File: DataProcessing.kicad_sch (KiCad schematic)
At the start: 2 parts, among them J3 AVR-ISP-6, U2 ATmega328PB-M

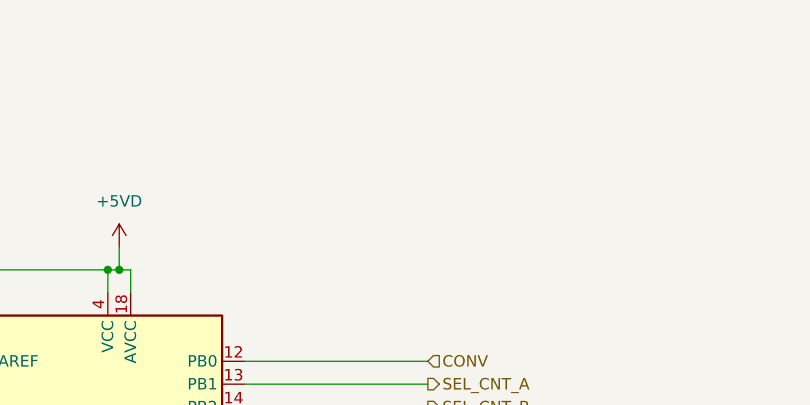
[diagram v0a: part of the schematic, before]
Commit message: added decoupling Cs
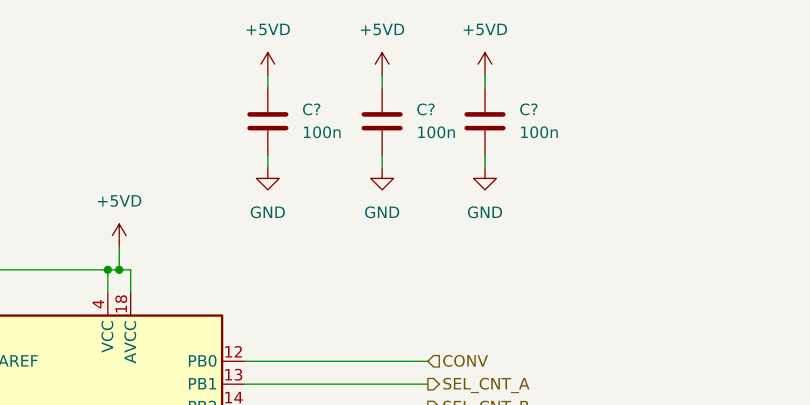
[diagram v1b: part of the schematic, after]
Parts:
- added C? (x3): 100n, Capacitor_SMD:C_0603_1608Metric, symbol Device:C
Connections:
- net +5VD: now also C?.1, C?.1, C?.1
- net GND: now also C?.2, C?.2, C?.2
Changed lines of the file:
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@@
   (junction (at 92.71 53.34) (diameter 0) (color 0 0 0 0)
   )
+  (wire (pts (xy 121.92 40.64) (xy 121.92 41.91))
+    (stroke (width 0) (type default) (color 0 0 0 0))
+  )
+  (wire (pts (xy 133.35 31.75) (xy 133.35 33.02))
+    (stroke (width 0) (type default) (color 0 0 0 0))
+  )
   (wire (pts (xy 74.93 53.34) (xy 91.44 53.34))
     (stroke (width 0) (type default) (color 0 0 0 0))
@@
     (stroke (width 0) (type default) (color 0 0 0 0))
   )
+  (wire (pts (xy 109.22 40.64) (xy 109.22 41.91))
+    (stroke (width 0) (type default) (color 0 0 0 0))
+  )
   (wire (pts (xy 91.44 55.88) (xy 91.44 53.34))
     (stroke (width 0) (type default) (color 0 0 0 0))
@@
     (stroke (width 0) (type default) (color 0 0 0 0))
   )
+  (wire (pts (xy 121.92 31.75) (xy 121.92 33.02))
+    (stroke (width 0) (type default) (color 0 0 0 0))
+  )
   (wire (pts (xy 106.68 109.22) (xy 127 109.22))
     (stroke (width 0) (type default) (color 0 0 0 0))
@@
     (stroke (width 0) (type default) (color 0 0 0 0))
   )
+  (wire (pts (xy 133.35 40.64) (xy 133.35 41.91))
+    (stroke (width 0) (type default) (color 0 0 0 0))
+  )
   (wire (pts (xy 106.68 106.68) (xy 127 106.68))
     (stroke (width 0) (type default) (color 0 0 0 0))
@@
   )
   (wire (pts (xy 106.68 96.52) (xy 127 96.52))
+    (stroke (width 0) (type default) (color 0 0 0 0))
+  )
+  (wire (pts (xy 109.22 31.75) (xy 109.22 33.02))
     (stroke (width 0) (type default) (color 0 0 0 0))
   )
@@
     (effects (font (size 1.27 1.27)) (justify left))
   )
+  (symbol (lib_id "power:GND") (at 109.22 41.91 0) (unit 1)
+    (in_bom yes) (on_board yes) (fields_autoplaced)
+    (property "Reference" "#PWR?" (id 0) (at 109.22 48.26 0)
+      (effects (font (size 1.27 1.27)) hide)
+    )
+    (property "Value" "GND" (id 1) (at 109.22 46.99 0))
+    (property "Footprint" "" (id 2) (at 109.22 41.91 0)
+      (effects (font (size 1.27 1.27)) hide)
+    )
+    (property "Datasheet" "" (id 3) (at 109.22 41.91 0)
+      (effects (font (size 1.27 1.27)) hide)
+    )
+    (pin "1")
+  )
+  (symbol (lib_id "power:+5VD") (at 109.22 31.75 0) (unit 1)
+    (in_bom yes) (on_board yes) (fields_autoplaced)
+    (property "Reference" "#PWR?" (id 0) (at 109.22 35.56 0)
+      (effects (font (size 1.27 1.27)) hide)
+    )
+    (property "Value" "+5VD" (id 1) (at 109.22 26.67 0))
+    (property "Footprint" "" (id 2) (at 109.22 31.75 0)
+      (effects (font (size 1.27 1.27)) hide)
+    )
+    (property "Datasheet" "" (id 3) (at 109.22 31.75 0)
+      (effects (font (size 1.27 1.27)) hide)
+    )
+    (pin "1")
+  )
+  (symbol (lib_id "Device:C") (at 121.92 36.83 0) (unit 1)
+    (in_bom yes) (on_board yes) (fields_autoplaced)
+    (property "Reference" "C?" (id 0) (at 125.73 35.5599 0)
+      (effects (font (size 1.27 1.27)) (justify left))
+    )
+    (property "Value" "100n" (id 1) (at 125.73 38.0999 0)
+      (effects (font (size 1.27 1.27)) (justify left))
+    )
+    (property "Footprint" "Capacitor_SMD:C_0603_1608Metric" (id 2) (at 122.8852 40.64 0)
+      (effects (font (size 1.27 1.27)) hide)
+    )
+    (property "Datasheet" "~" (id 3) (at 121.92 36.83 0)
+      (effects (font (size 1.27 1.27)) hide)
+    )
+    (pin "1")
+    (pin "2")
+  )
   (symbol (lib_id "power:+5VD") (at 232.41 40.64 0) (unit 1)
     (in_bom yes) (on_board yes) (fields_autoplaced)
@@
     )
     (property "Datasheet" "" (id 3) (at 91.44 139.7 0)
+      (effects (font (size 1.27 1.27)) hide)
+    )
+    (pin "1")
+  )
+  (symbol (lib_id "Device:C") (at 133.35 36.83 0) (unit 1)
+    (in_bom yes) (on_board yes) (fields_autoplaced)
+    (property "Reference" "C?" (id 0) (at 137.16 35.5599 0)
+      (effects (font (size 1.27 1.27)) (justify left))
+    )
+    (property "Value" "100n" (id 1) (at 137.16 38.0999 0)
+      (effects (font (size 1.27 1.27)) (justify left))
+    )
+    (property "Footprint" "Capacitor_SMD:C_0603_1608Metric" (id 2) (at 134.3152 40.64 0)
+      (effects (font (size 1.27 1.27)) hide)
+    )
+    (property "Datasheet" "~" (id 3) (at 133.35 36.83 0)
+      (effects (font (size 1.27 1.27)) hide)
+    )
+    (pin "1")
+    (pin "2")
+  )
+  (symbol (lib_id "Device:C") (at 109.22 36.83 0) (unit 1)
+    (in_bom yes) (on_board yes) (fields_autoplaced)
+    (property "Reference" "C?" (id 0) (at 113.03 35.5599 0)
+      (effects (font (size 1.27 1.27)) (justify left))
+    )
+    (property "Value" "100n" (id 1) (at 113.03 38.0999 0)
+      (effects (font (size 1.27 1.27)) (justify left))
+    )
+    (property "Footprint" "Capacitor_SMD:C_0603_1608Metric" (id 2) (at 110.1852 40.64 0)
+      (effects (font (size 1.27 1.27)) hide)
+    )
+    (property "Datasheet" "~" (id 3) (at 109.22 36.83 0)
+      (effects (font (size 1.27 1.27)) hide)
+    )
+    (pin "1")
+    (pin "2")
+  )
+  (symbol (lib_id "power:+5VD") (at 133.35 31.75 0) (unit 1)
+    (in_bom yes) (on_board yes) (fields_autoplaced)
+    (property "Reference" "#PWR?" (id 0) (at 133.35 35.56 0)
+      (effects (font (size 1.27 1.27)) hide)
+    )
+    (property "Value" "+5VD" (id 1) (at 133.35 26.67 0))
+    (property "Footprint" "" (id 2) (at 133.35 31.75 0)
+      (effects (font (size 1.27 1.27)) hide)
+    )
+    (property "Datasheet" "" (id 3) (at 133.35 31.75 0)
       (effects (font (size 1.27 1.27)) hide)
     )
@@
     (pin "5")
     (pin "6")
+  )
+  (symbol (lib_id "power:GND") (at 121.92 41.91 0) (unit 1)
+    (in_bom yes) (on_board yes) (fields_autoplaced)
+    (property "Reference" "#PWR?" (id 0) (at 121.92 48.26 0)
+      (effects (font (size 1.27 1.27)) hide)
+    )
+    (property "Value" "GND" (id 1) (at 121.92 46.99 0))
+    (property "Footprint" "" (id 2) (at 121.92 41.91 0)
+      (effects (font (size 1.27 1.27)) hide)
+    )
+    (property "Datasheet" "" (id 3) (at 121.92 41.91 0)
+      (effects (font (size 1.27 1.27)) hide)
+    )
+    (pin "1")
+  )
+  (symbol (lib_id "power:+5VD") (at 121.92 31.75 0) (unit 1)
+    (in_bom yes) (on_board yes) (fields_autoplaced)
+    (property "Reference" "#PWR?" (id 0) (at 121.92 35.56 0)
+      (effects (font (size 1.27 1.27)) hide)
+    )
+    (property "Value" "+5VD" (id 1) (at 121.92 26.67 0))
+    (property "Footprint" "" (id 2) (at 121.92 31.75 0)
+      (effects (font (size 1.27 1.27)) hide)
+    )
+    (property "Datasheet" "" (id 3) (at 121.92 31.75 0)
+      (effects (font (size 1.27 1.27)) hide)
+    )
+    (pin "1")
   )
   (symbol (lib_id "MCU_Microchip_ATmega:ATmega328PB-M") (at 91.44 93.98 0) (unit 1)
@@
     (pin "9")
   )
+  (symbol (lib_id "power:GND") (at 133.35 41.91 0) (unit 1)
+    (in_bom yes) (on_board yes) (fields_autoplaced)
+    (property "Reference" "#PWR?" (id 0) (at 133.35 48.26 0)
+      (effects (font (size 1.27 1.27)) hide)
+    )
+    (property "Value" "GND" (id 1) (at 133.35 46.99 0))
+    (property "Footprint" "" (id 2) (at 133.35 41.91 0)
+      (effects (font (size 1.27 1.27)) hide)
+    )
+    (property "Datasheet" "" (id 3) (at 133.35 41.91 0)
+      (effects (font (size 1.27 1.27)) hide)
+    )
+    (pin "1")
+  )
   (symbol (lib_id "power:+5VD") (at 92.71 50.8 0) (unit 1)

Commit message: changed title block to meaningful information
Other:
- title: (none) -> Open Nano Amp Meter
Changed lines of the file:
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@@
 (kicad_sch (version 20211123) (generator eeschema)
   (paper "A4")
+  (title_block
+    (title "Open Nano Amp Meter")
+    (date "2022-11-17")
+    (rev "0.9")
+  )
   (junction (at 91.44 53.34) (diameter 0) (color 0 0 0 0)
   )

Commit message: added 2 LEDs for some status output
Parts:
- added D1, D2: LED, LED_SMD:LED_0603_1608Metric, symbol Device:LED
- added R10, R9: R, Resistor_SMD:R_0402_1005Metric, symbol Device:R
- gave numbers to parts that had none: 3
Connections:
- net +5VD: now also R10.1, R9.1
- net at U2.19 (PE2): now also D2.1 (K)
- net at U2.22 (PE3): now also D1.1 (K)
- new net: D1.2 (A), R9.2
- new net: D2.2 (A), R10.2
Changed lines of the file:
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@@
+    (stroke (width 0) (type default) (color 0 0 0 0))
+  )
+  (wire (pts (xy 39.37 114.3) (xy 39.37 109.22))
     (stroke (width 0) (type default) (color 0 0 0 0))
   )
@@
     (stroke (width 0) (type default) (color 0 0 0 0))
   )
-  (wire (pts (xy 55.88 114.3) (xy 76.2 114.3))
+  (wire (pts (xy 39.37 114.3) (xy 76.2 114.3))
     (stroke (width 0) (type default) (color 0 0 0 0))
   )
@@
     (stroke (width 0) (type default) (color 0 0 0 0))
   )
+  (wire (pts (xy 39.37 99.06) (xy 39.37 101.6))
+    (stroke (width 0) (type default) (color 0 0 0 0))
+  )
   (wire (pts (xy 106.68 81.28) (xy 127 81.28))
     (stroke (width 0) (type default) (color 0 0 0 0))
   )
-  (wire (pts (xy 55.88 111.76) (xy 76.2 111.76))
+  (wire (pts (xy 50.8 111.76) (xy 76.2 111.76))
     (stroke (width 0) (type default) (color 0 0 0 0))
   )
@@
     (stroke (width 0) (type default) (color 0 0 0 0))
   )
+  (wire (pts (xy 39.37 87.63) (xy 39.37 91.44))
+    (stroke (width 0) (type default) (color 0 0 0 0))
+  )
   (wire (pts (xy 106.68 109.22) (xy 127 109.22))
     (stroke (width 0) (type default) (color 0 0 0 0))
@@
     (stroke (width 0) (type default) (color 0 0 0 0))
   )
+  (wire (pts (xy 50.8 99.06) (xy 50.8 101.6))
+    (stroke (width 0) (type default) (color 0 0 0 0))
+  )
   (wire (pts (xy 92.71 50.8) (xy 92.71 53.34))
     (stroke (width 0) (type default) (color 0 0 0 0))
@@
     (stroke (width 0) (type default) (color 0 0 0 0))
   )
-  (wire (pts (xy 55.88 106.68) (xy 76.2 106.68))
+  (wire (pts (xy 72.39 106.68) (xy 76.2 106.68))
     (stroke (width 0) (type default) (color 0 0 0 0))
   )
@@
     (stroke (width 0) (type default) (color 0 0 0 0))
   )
-  (wire (pts (xy 55.88 109.22) (xy 76.2 109.22))
+  (wire (pts (xy 72.39 109.22) (xy 76.2 109.22))
     (stroke (width 0) (type default) (color 0 0 0 0))
   )
@@
     (stroke (width 0) (type default) (color 0 0 0 0))
   )
+  (wire (pts (xy 50.8 87.63) (xy 50.8 91.44))
+    (stroke (width 0) (type default) (color 0 0 0 0))
+  )
   (wire (pts (xy 133.35 40.64) (xy 133.35 41.91))
     (stroke (width 0) (type default) (color 0 0 0 0))
@@
     (stroke (width 0) (type default) (color 0 0 0 0))
   )
+  (wire (pts (xy 50.8 111.76) (xy 50.8 109.22))
+    (stroke (width 0) (type default) (color 0 0 0 0))
+  )
   (wire (pts (xy 212.09 55.88) (xy 219.71 55.88))
     (stroke (width 0) (type default) (color 0 0 0 0))
@@
     (effects (font (size 1.27 1.27)) (justify left))
   )
-  (hierarchical_label "TEST" (shape output) (at 55.88 109.22 180)
+  (hierarchical_label "TEST" (shape output) (at 72.39 109.22 180)
     (effects (font (size 1.27 1.27)) (justify right))
   )
@@
     (effects (font (size 1.27 1.27)) (justify left))
   )
-  (hierarchical_label "MUX_SEL_2" (shape output) (at 55.88 106.68 180)
+  (hierarchical_label "MUX_SEL_2" (shape output) (at 72.39 106.68 180)
     (effects (font (size 1.27 1.27)) (justify right))
   )
@@
     (effects (font (size 1.27 1.27)) (justify left))
   )
+  (symbol (lib_id "Device:R") (at 39.37 95.25 0) (unit 1)
+    (in_bom yes) (on_board yes) (fields_autoplaced)
+    (property "Reference" "R9" (id 0) (at 41.91 93.9799 0)
+      (effects (font (size 1.27 1.27)) (justify left))
+    )
+    (property "Value" "R" (id 1) (at 41.91 96.5199 0)
+      (effects (font (size 1.27 1.27)) (justify left))
+    )
+    (property "Footprint" "Resistor_SMD:R_0402_1005Metric" (id 2) (at 37.592 95.25 90)
+      (effects (font (size 1.27 1.27)) hide)
+    )
+    (property "Datasheet" "~" (id 3) (at 39.37 95.25 0)
+      (effects (font (size 1.27 1.27)) hide)
+    )
+    (pin "1")
+    (pin "2")
+  )
+  (symbol (lib_id "Device:LED") (at 39.37 105.41 90) (unit 1)
+    (in_bom yes) (on_board yes) (fields_autoplaced)
+    (property "Reference" "D1" (id 0) (at 43.18 105.7274 90)
+      (effects (font (size 1.27 1.27)) (justify right))
+    )
+    (property "Value" "LED" (id 1) (at 43.18 108.2674 90)
+      (effects (font (size 1.27 1.27)) (justify right))
+    )
+    (property "Footprint" "LED_SMD:LED_0603_1608Metric" (id 2) (at 39.37 105.41 0)
+      (effects (font (size 1.27 1.27)) hide)
+    )
+    (property "Datasheet" "~" (id 3) (at 39.37 105.41 0)
+      (effects (font (size 1.27 1.27)) hide)
+    )
+    (pin "1")
+    (pin "2")
+  )
   (symbol (lib_id "power:GND") (at 109.22 41.91 0) (unit 1)
     (in_bom yes) (on_board yes) (fields_autoplaced)
-    (property "Reference" "#PWR?" (id 0) (at 109.22 48.26 0)
+    (property "Reference" "#PWR019" (id 0) (at 109.22 48.26 0)
       (effects (font (size 1.27 1.27)) hide)
     )
@@
     (pin "1")
   )
+  (symbol (lib_id "power:+5VD") (at 50.8 87.63 0) (unit 1)
+    (in_bom yes) (on_board yes) (fields_autoplaced)
+    (property "Reference" "#PWR031" (id 0) (at 50.8 91.44 0)
+      (effects (font (size 1.27 1.27)) hide)
+    )
+    (property "Value" "+5VD" (id 1) (at 50.8 82.55 0))
+    (property "Footprint" "" (id 2) (at 50.8 87.63 0)
+      (effects (font (size 1.27 1.27)) hide)
+    )
+    (property "Datasheet" "" (id 3) (at 50.8 87.63 0)
+      (effects (font (size 1.27 1.27)) hide)
+    )
+    (pin "1")
+  )
   (symbol (lib_id "power:+5VD") (at 109.22 31.75 0) (unit 1)
     (in_bom yes) (on_board yes) (fields_autoplaced)
-    (property "Reference" "#PWR?" (id 0) (at 109.22 35.56 0)
+    (property "Reference" "#PWR018" (id 0) (at 109.22 35.56 0)
       (effects (font (size 1.27 1.27)) hide)
     )
@@
   (symbol (lib_id "Device:C") (at 121.92 36.83 0) (unit 1)
     (in_bom yes) (on_board yes) (fields_autoplaced)
-    (property "Reference" "C?" (id 0) (at 125.73 35.5599 0)
+    (property "Reference" "C13" (id 0) (at 125.73 35.5599 0)
       (effects (font (size 1.27 1.27)) (justify left))
     )
@@
     )
     (property "Datasheet" "~" (id 3) (at 121.92 36.83 0)
+      (effects (font (size 1.27 1.27)) hide)
+    )
+    (pin "1")
+    (pin "2")
+  )
+  (symbol (lib_id "Device:LED") (at 50.8 105.41 90) (unit 1)
+    (in_bom yes) (on_board yes) (fields_autoplaced)
+    (property "Reference" "D2" (id 0) (at 54.61 105.7274 90)
+      (effects (font (size 1.27 1.27)) (justify right))
+    )
+    (property "Value" "LED" (id 1) (at 54.61 108.2674 90)
+      (effects (font (size 1.27 1.27)) (justify right))
+    )
+    (property "Footprint" "LED_SMD:LED_0603_1608Metric" (id 2) (at 50.8 105.41 0)
+      (effects (font (size 1.27 1.27)) hide)
+    )
+    (property "Datasheet" "~" (id 3) (at 50.8 105.41 0)
       (effects (font (size 1.27 1.27)) hide)
     )
@@
   (symbol (lib_id "Device:C") (at 133.35 36.83 0) (unit 1)
     (in_bom yes) (on_board yes) (fields_autoplaced)
-    (property "Reference" "C?" (id 0) (at 137.16 35.5599 0)
+    (property "Reference" "C14" (id 0) (at 137.16 35.5599 0)
       (effects (font (size 1.27 1.27)) (justify left))
     )
@@
   (symbol (lib_id "Device:C") (at 109.22 36.83 0) (unit 1)
     (in_bom yes) (on_board yes) (fields_autoplaced)
-    (property "Reference" "C?" (id 0) (at 113.03 35.5599 0)
+    (property "Reference" "C12" (id 0) (at 113.03 35.5599 0)
       (effects (font (size 1.27 1.27)) (justify left))
     )
@@
     (pin "2")
   )
+  (symbol (lib_id "Device:R") (at 50.8 95.25 0) (unit 1)
+    (in_bom yes) (on_board yes) (fields_autoplaced)
+    (property "Reference" "R10" (id 0) (at 53.34 93.9799 0)
+      (effects (font (size 1.27 1.27)) (justify left))
+    )
+    (property "Value" "R" (id 1) (at 53.34 96.5199 0)
+      (effects (font (size 1.27 1.27)) (justify left))
+    )
+    (property "Footprint" "Resistor_SMD:R_0402_1005Metric" (id 2) (at 49.022 95.25 90)
+      (effects (font (size 1.27 1.27)) hide)
+    )
+    (property "Datasheet" "~" (id 3) (at 50.8 95.25 0)
+      (effects (font (size 1.27 1.27)) hide)
+    )
+    (pin "1")
+    (pin "2")
+  )
   (symbol (lib_id "power:+5VD") (at 133.35 31.75 0) (unit 1)
     (in_bom yes) (on_board yes) (fields_autoplaced)
-    (property "Reference" "#PWR?" (id 0) (at 133.35 35.56 0)
+    (property "Reference" "#PWR022" (id 0) (at 133.35 35.56 0)
       (effects (font (size 1.27 1.27)) hide)
     )
@@
   (symbol (lib_id "power:GND") (at 121.92 41.91 0) (unit 1)
     (in_bom yes) (on_board yes) (fields_autoplaced)
-    (property "Reference" "#PWR?" (id 0) (at 121.92 48.26 0)
+    (property "Reference" "#PWR021" (id 0) (at 121.92 48.26 0)
       (effects (font (size 1.27 1.27)) hide)
     )
@@
   (symbol (lib_id "power:+5VD") (at 121.92 31.75 0) (unit 1)
     (in_bom yes) (on_board yes) (fields_autoplaced)
-    (property "Reference" "#PWR?" (id 0) (at 121.92 35.56 0)
+    (property "Reference" "#PWR020" (id 0) (at 121.92 35.56 0)
       (effects (font (size 1.27 1.27)) hide)
     )
@@
   (symbol (lib_id "power:GND") (at 133.35 41.91 0) (unit 1)
     (in_bom yes) (on_board yes) (fields_autoplaced)
-    (property "Reference" "#PWR?" (id 0) (at 133.35 48.26 0)
+    (property "Reference" "#PWR023" (id 0) (at 133.35 48.26 0)
       (effects (font (size 1.27 1.27)) hide)
     )
@@
       (effects (font (size 1.27 1.27)) hide)
     )
+    (pin "1")
+  )
+  (symbol (lib_id "power:+5VD") (at 39.37 87.63 0) (unit 1)
+    (in_bom yes) (on_board yes) (fields_autoplaced)
+    (property "Reference" "#PWR030" (id 0) (at 39.37 91.44 0)
+      (effects (font (size 1.27 1.27)) hide)
+    )
+    (property "Value" "+5VD" (id 1) (at 39.37 82.55 0))
+    (property "Footprint" "" (id 2) (at 39.37 87.63 0)
+      (effects (font (size 1.27 1.27)) hide)
+    )
+    (property "Datasheet" "" (id 3) (at 39.37 87.63 0)
+      (effects (font (size 1.27 1.27)) hide)
+    )

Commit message: changed resistor footprint to 0603
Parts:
- R10, R9: footprint Resistor_SMD:R_0402_1005Metric -> Resistor_SMD:R_0603_1608Metric
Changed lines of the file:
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@@
       (effects (font (size 1.27 1.27)) (justify left))
     )
-    (property "Footprint" "Resistor_SMD:R_0402_1005Metric" (id 2) (at 37.592 95.25 90)
+    (property "Footprint" "Resistor_SMD:R_0603_1608Metric" (id 2) (at 37.592 95.25 90)
       (effects (font (size 1.27 1.27)) hide)
     )
@@
       (effects (font (size 1.27 1.27)) (justify left))
     )
-    (property "Footprint" "Resistor_SMD:R_0402_1005Metric" (id 2) (at 49.022 95.25 90)
+    (property "Footprint" "Resistor_SMD:R_0603_1608Metric" (id 2) (at 49.022 95.25 90)
       (effects (font (size 1.27 1.27)) hide)
     )

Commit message: changed setting of clock divider to I2C
reduces pin load on uC, thus frees pins for usage with other functions.
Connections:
- net MUX_SEL_0 is gone; now on net RX: U2.1 (PD3)
- net MUX_SEL_1 is gone; now on net TX: U2.2 (PD4)
- net SEL_CNT_A is gone; now on net CNT_CLR: U2.13 (PB1)
- net CNT_CLR: no longer U2.32 (PD2)
- net RX: no longer U2.31 (PD1)
- net TX: no longer U2.30 (PD0)
- net MUX_SEL_2: no longer names the net of U2.3 (PE0)
- net SEL_CNT_B: no longer names the net of U2.14 (PB2)
- new net RXD0: U2.31 (PD1)
- new net TXD0: U2.30 (PD0)
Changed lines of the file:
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@@
     (effects (font (size 1.27 1.27)) (justify left bottom))
   )
-  (hierarchical_label "SEL_CNT_A" (shape output) (at 127 66.04 0)
+  (hierarchical_label "DOUT" (shape input) (at 127 86.36 0)
     (effects (font (size 1.27 1.27)) (justify left))
   )
-  (hierarchical_label "DOUT" (shape input) (at 127 86.36 0)
+  (hierarchical_label "RX" (shape input) (at 127 114.3 0)
     (effects (font (size 1.27 1.27)) (justify left))
   )
@@
     (effects (font (size 1.27 1.27)) (justify left))
   )
-  (hierarchical_label "SEL_CNT_B" (shape output) (at 127 68.58 0)
-    (effects (font (size 1.27 1.27)) (justify left))
-  )
   (hierarchical_label "TEST" (shape output) (at 72.39 109.22 180)
     (effects (font (size 1.27 1.27)) (justify right))
   )
-  (hierarchical_label "RX" (shape input) (at 127 109.22 0)
+  (hierarchical_label "TX" (shape output) (at 127 116.84 0)
     (effects (font (size 1.27 1.27)) (justify left))
   )
@@
     (effects (font (size 1.27 1.27)) (justify left))
   )
-  (hierarchical_label "MUX_SEL_2" (shape output) (at 72.39 106.68 180)
-    (effects (font (size 1.27 1.27)) (justify right))
-  )
   (hierarchical_label "DCLK" (shape output) (at 127 88.9 0)
     (effects (font (size 1.27 1.27)) (justify left))
   )
-  (hierarchical_label "MUX_SEL_1" (shape output) (at 127 116.84 0)
+  (hierarchical_label "SDA" (shape bidirectional) (at 127 96.52 0)
     (effects (font (size 1.27 1.27)) (justify left))
   )
@@
     (effects (font (size 1.27 1.27)) (justify left))
   )
+  (hierarchical_label "SCL" (shape output) (at 127 99.06 0)
+    (effects (font (size 1.27 1.27)) (justify left))
+  )
   (hierarchical_label "RANGE0" (shape output) (at 127 119.38 0)
     (effects (font (size 1.27 1.27)) (justify left))
   )
-  (hierarchical_label "MUX_SEL_0" (shape output) (at 127 114.3 0)
-    (effects (font (size 1.27 1.27)) (justify left))
-  )
-  (hierarchical_label "TX" (shape output) (at 127 106.68 0)
+  (hierarchical_label "CNT_CLR" (shape output) (at 127 66.04 0)
     (effects (font (size 1.27 1.27)) (justify left))
   )
@@
     (effects (font (size 1.27 1.27)) (justify left))
   )
-  (hierarchical_label "CNT_CLR" (shape output) (at 127 111.76 0)
-    (effects (font (size 1.27 1.27)) (justify left))
-  )
